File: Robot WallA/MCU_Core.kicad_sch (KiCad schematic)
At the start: 16 parts, among them IC1 STM32F407IGT6, IC2 DS04-254-2-04BK-SMT, J1 Conn_02x05_Female, Y1 Crystal_GND24

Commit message: Correct a lot of error in DRC
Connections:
- net PE2 is gone; now on net LED_Red: IC1.1 (PE2)
- net PE3 is gone; now on net LED_Blue: IC1.2 (PE3)
- net PE4 is gone; now on net LED_Green: IC1.3 (PE4)
- net PE5 is gone; now on net LED_Orange: IC1.4 (PE5)
- net PE6 is gone; now on net LED_Yellow: IC1.5 (PE6)
- no-connect marks 4 -> 8
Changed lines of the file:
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@@
 	)
 	(no_connect
+		(at 68.58 237.49)
+	)
+	(no_connect
 		(at 41.91 116.84)
 	)
@@
 	)
 	(no_connect
+		(at 68.58 234.95)
+	)
+	(no_connect
 		(at 55.88 116.84)
 	)
@@
 		(at 55.88 113.03)
 	)
-	(bus_entry
-		(at 364.49 62.23)
-		(size -2.54 2.54)
-		(stroke
-			(width 0)
-			(type default)
-		)
+	(no_connect
+		(at 68.58 240.03)
+	)
+	(no_connect
+		(at 68.58 242.57)
 	)
 	(bus_entry
@@
 	)
 	(bus_entry
-		(at 364.49 59.69)
-		(size -2.54 2.54)
-		(stroke
-			(width 0)
-			(type default)
-		)
-	)
-	(bus_entry
 		(at 387.35 34.29)
 		(size 2.54 2.54)
@@
 	)
 	(bus_entry
-		(at 364.49 64.77)
-		(size -2.54 2.54)
-		(stroke
-			(width 0)
-			(type default)
-		)
-	)
-	(bus_entry
 		(at 342.9 67.31)
 		(size 2.54 2.54)
@@
 	)
 	(bus_entry
-		(at 364.49 67.31)
-		(size -2.54 2.54)
-		(stroke
-			(width 0)
-			(type default)
-		)
-	)
-	(bus_entry
 		(at 339.09 237.49)
 		(size -2.54 2.54)
@@
 	)
 	(bus_entry
-		(at 364.49 57.15)
-		(size -2.54 2.54)
-		(stroke
-			(width 0)
-			(type default)
-		)
-	)
-	(bus_entry
 		(at 364.49 95.25)
 		(size -2.54 2.54)
@@
 	(wire
 		(pts
-			(xy 360.68 64.77) (xy 361.95 64.77)
-		)
-		(stroke
-			(width 0)
-			(type default)
-		)
-	)
-	(wire
-		(pts
 			(xy 35.56 160.02) (xy 38.1 160.02)
 		)
@@
 	(bus
 		(pts
-			(xy 364.49 64.77) (xy 364.49 67.31)
-		)
-		(stroke
-			(width 0)
-			(type default)
-		)
-	)
-	(bus
-		(pts
 			(xy 365.76 76.2) (xy 364.49 76.2)
 		)
@@
 		)
 	)
-	(wire
-		(pts
-			(xy 360.68 67.31) (xy 361.95 67.31)
-		)
-		(stroke
-			(width 0)
-			(type default)
-		)
-	)
 	(bus
 		(pts
@@
 		)
 	)
-	(bus
-		(pts
-			(xy 364.49 57.15) (xy 364.49 59.69)
-		)
-		(stroke
-			(width 0)
-			(type default)
-		)
-	)
 	(wire
 		(pts
@@
 		)
 	)
-	(bus
-		(pts
-			(xy 364.49 67.31) (xy 364.49 69.85)
-		)
-		(stroke
-			(width 0)
-			(type default)
-		)
-	)
 	(wire
 		(pts
@@
 		)
 	)
-	(wire
-		(pts
-			(xy 360.68 62.23) (xy 361.95 62.23)
-		)
-		(stroke
-			(width 0)
-			(type default)
-		)
-	)
 	(bus
 		(pts
@@
 		)
 	)
-	(bus
-		(pts
-			(xy 364.49 62.23) (xy 364.49 64.77)
-		)
-		(stroke
-			(width 0)
-			(type default)
-		)
-	)
 	(wire
 		(pts
@@
 	(bus
 		(pts
-			(xy 364.49 54.61) (xy 364.49 57.15)
+			(xy 364.49 54.61) (xy 364.49 69.85)
 		)
 		(stroke
@@
 		)
 	)
-	(wire
-		(pts
-			(xy 360.68 69.85) (xy 361.95 69.85)
-		)
-		(stroke
-			(width 0)
-			(type default)
-		)
-	)
 	(bus
 		(pts
@@
 	(bus
 		(pts
-			(xy 364.49 59.69) (xy 364.49 62.23)
-		)
-		(stroke
-			(width 0)
-			(type default)
-		)
-	)
-	(bus
-		(pts
 			(xy 364.49 135.89) (xy 364.49 138.43)
 		)
@@
 	(wire
 		(pts
-			(xy 360.68 59.69) (xy 361.95 59.69)
-		)
-		(stroke
-			(width 0)
-			(type default)
-		)
-	)
-	(wire
-		(pts
 			(xy 354.33 130.81) (xy 361.95 130.81)
 		)
@@
 		)
 	)
-	(label "PE5"
-		(at 360.68 67.31 180)
-		(effects
-			(font
-				(size 1.27 1.27)
-			)
-			(justify right bottom)
-		)
-	)
 	(label "RMII_MDC"
 		(at 227.33 195.58 270)
@@
 	)
 	(label "LED_Blue"
-		(at 52.07 255.27 0)
+		(at 148.59 195.58 270)
 		(effects
 			(font
 				(size 1.27 1.27)
 			)
-			(justify left bottom)
+			(justify right bottom)
 		)
 	)
@@
 	)
 	(label "LED_Orange"
-		(at 52.07 260.35 0)
+		(at 153.67 195.58 270)
 		(effects
 			(font
 				(size 1.27 1.27)
 			)
-			(justify left bottom)
+			(justify right bottom)
 		)
 	)
@@
 		)
 	)
-	(label "PE6"
-		(at 156.21 195.58 270)
-		(effects
-			(font
-				(size 1.27 1.27)
-			)
-			(justify right bottom)
-		)
-	)
 	(label "PH8"
 		(at 278.13 86.36 0)
@@
 		)
 	)
-	(label "PE3"
-		(at 360.68 62.23 180)
-		(effects
-			(font
-				(size 1.27 1.27)
-			)
-			(justify right bottom)
-		)
-	)
 	(label "VDD"
 		(at 234.95 195.58 270)
@@
 		)
 	)
-	(label "PE4"
-		(at 360.68 64.77 180)
-		(effects
-			(font
-				(size 1.27 1.27)
-			)
-			(justify right bottom)
-		)
-	)
 	(label "PHY_CLK_25MHZ"
 		(at 179.07 71.12 90)
@@
 		)
 	)
-	(label "PE2"
-		(at 360.68 59.69 180)
-		(effects
-			(font
-				(size 1.27 1.27)
-			)
-			(justify right bottom)
-		)
-	)
 	(label "ETH1"
 		(at 360.68 123.19 180)
@@
 	)
 	(label "LED_Green"
-		(at 52.07 250.19 0)
+		(at 151.13 195.58 270)
 		(effects
 			(font
 				(size 1.27 1.27)
 			)
-			(justify left bottom)
+			(justify right bottom)
 		)
 	)
@@
 	)
 	(label "LED_Yellow"
-		(at 52.07 257.81 0)
+		(at 156.21 195.58 270)
 		(effects
 			(font
 				(size 1.27 1.27)
 			)
-			(justify left bottom)
+			(justify right bottom)
 		)
 	)
@@
 		)
 	)
-	(label "PE6"
-		(at 360.68 69.85 180)
-		(effects
-			(font
-				(size 1.27 1.27)
-			)
-			(justify right bottom)
-		)
-	)
 	(label "PF3"
 		(at 191.77 195.58 270)
@@
 		)
 	)
-	(label "PE3"
-		(at 148.59 195.58 270)
-		(effects
-			(font
-				(size 1.27 1.27)
-			)
-			(justify right bottom)
-		)
-	)
 	(label "Sensor_InputCapture4"
 		(at 181.61 71.12 90)
@@
 		)
 	)
-	(label "PE2"
-		(at 146.05 195.58 270)
-		(effects
-			(font
-				(size 1.27 1.27)
-			)
-			(justify right bottom)
-		)
-	)
 	(label "SWCLK"
 		(at 128.27 88.9 180)
@@
 		)
 	)
-	(label "PE5"
-		(at 153.67 195.58 270)
-		(effects
-			(font
-				(size 1.27 1.27)
-			)
-			(justify right bottom)
-		)
-	)
 	(label "PD14"
 		(at 346.71 69.85 0)
@@
 	)
 	(label "LED_Red"
-		(at 52.07 252.73 0)
+		(at 146.05 195.58 270)
 		(effects
 			(font
 				(size 1.27 1.27)
 			)
-			(justify left bottom)
+			(justify right bottom)
 		)
 	)
@@
 		(effects
 			(font
-				(size 1.27 1.27)
-			)
-			(justify right bottom)
-		)
-	)
-	(label "PE4"
-		(at 151.13 195.58 270)
-		(effects
-			(font

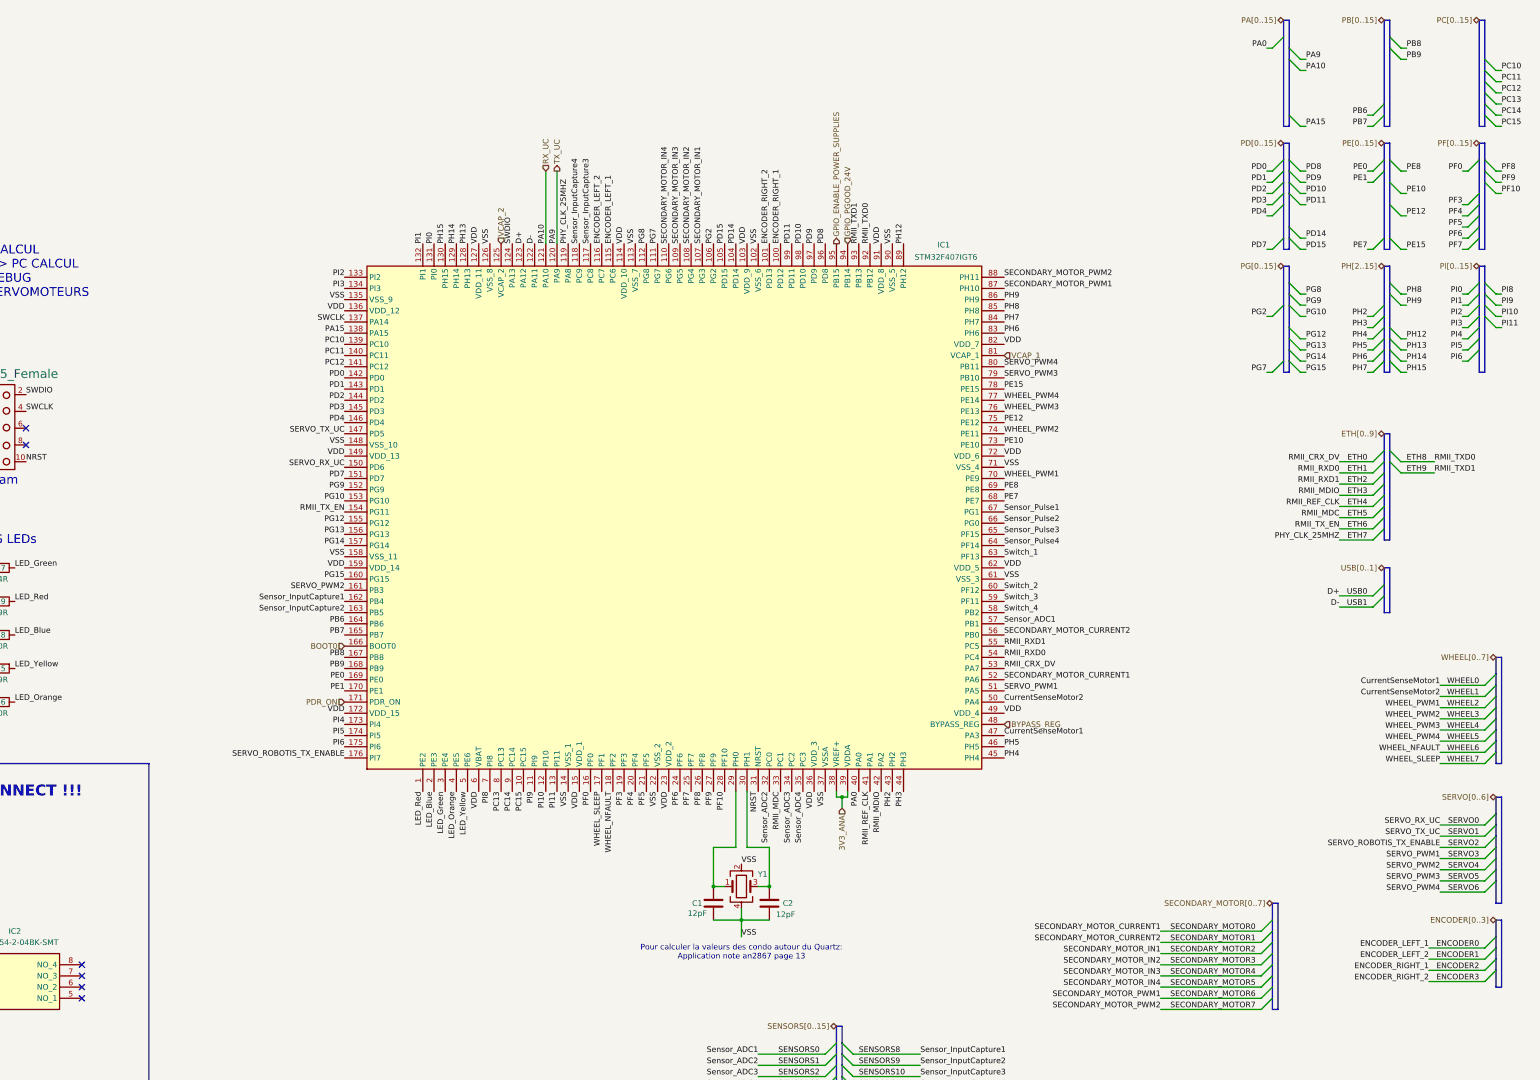
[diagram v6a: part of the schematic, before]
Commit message: Corrected all DRC erros, added info on PCB
modified distance meter connectors to be horizontal
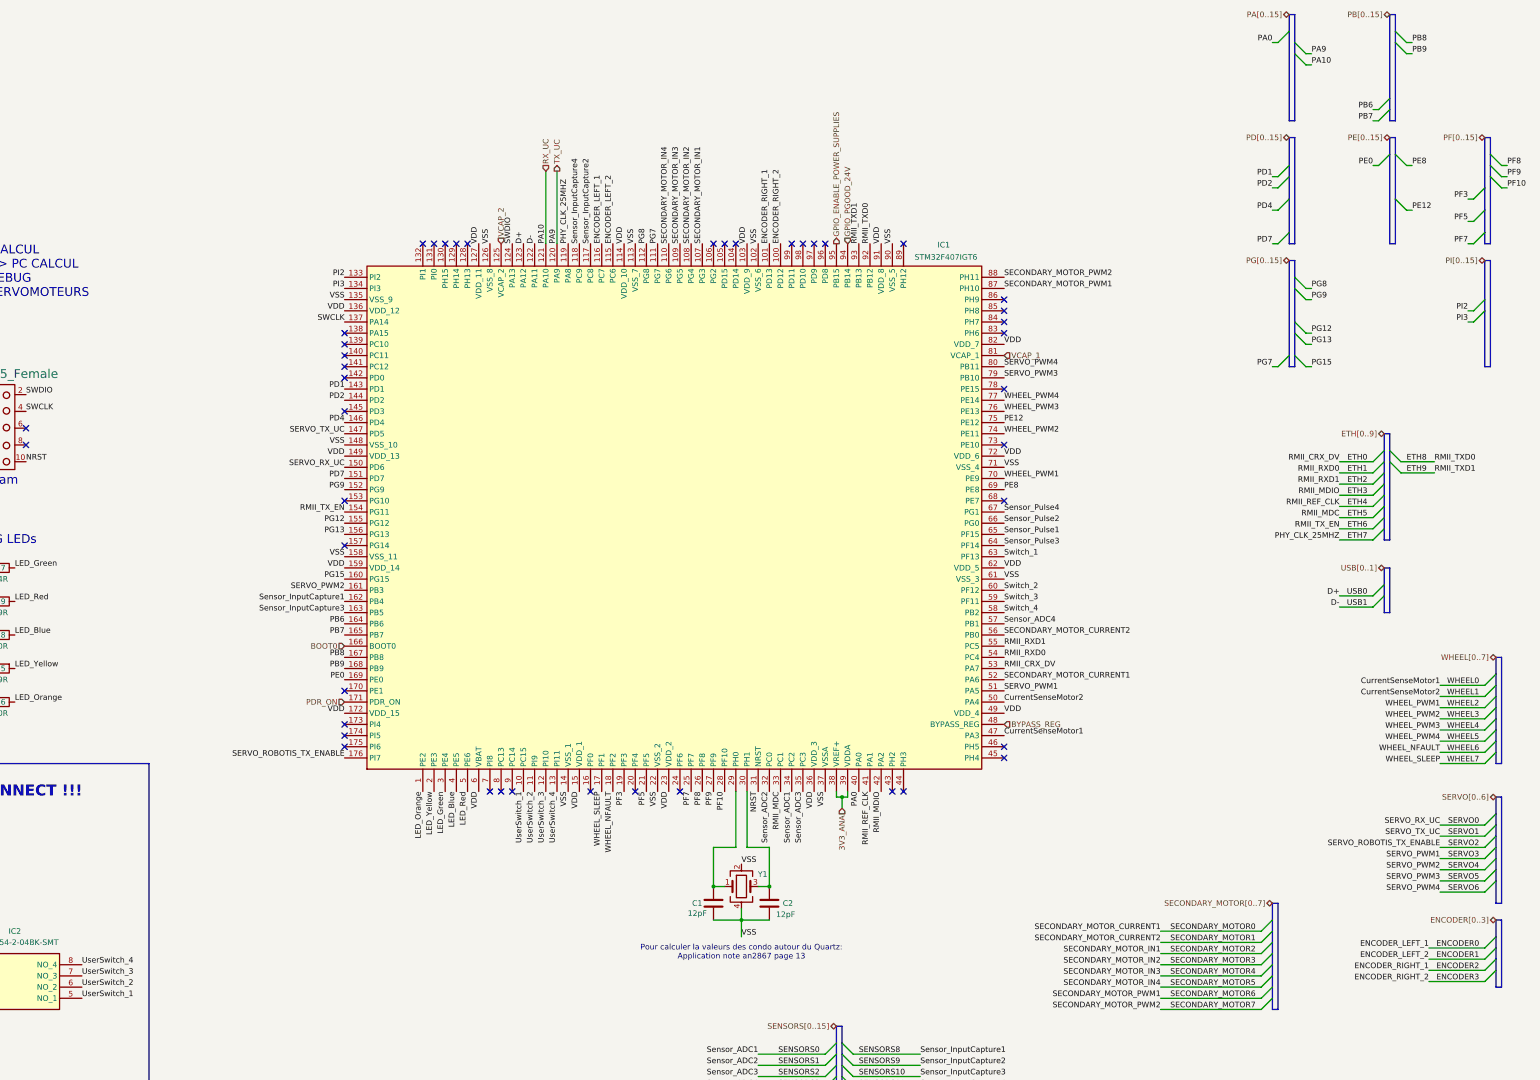
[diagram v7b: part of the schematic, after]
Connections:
- net PC15 is gone; now on net UserSwitch_1: IC1.10 (PC15)
- net PI10 is gone; now on net UserSwitch_3: IC1.12 (PI10)
- net PI11 is gone; now on net UserSwitch_4: IC1.13 (PI11)
- net PI9 is gone; now on net UserSwitch_2: IC1.11 (PI9)
- net ENCODER0: now also IC1.116 (PC7); no longer IC1.115 (PC6)
- net ENCODER1: now also IC1.115 (PC6); no longer IC1.116 (PC7)
- net ENCODER2: now also IC1.101 (PD13); no longer IC1.100 (PD12)
- net ENCODER3: now also IC1.100 (PD12); no longer IC1.101 (PD13)
- net LED_Blue: now also IC1.4 (PE5); no longer IC1.2 (PE3)
- net LED_Orange: now also IC1.1 (PE2); no longer IC1.4 (PE5)
- net LED_Red: now also IC1.5 (PE6); no longer IC1.1 (PE2)
- net LED_Yellow: now also IC1.2 (PE3); no longer IC1.5 (PE6)
- net SENSORS0: now also IC1.34 (PC2); no longer IC1.57 (PB1)
- net SENSORS10: now also IC1.163 (PB5); no longer IC1.117 (PC8)
- net SENSORS2: now also IC1.35 (PC3); no longer IC1.34 (PC2)
- net SENSORS3: now also IC1.57 (PB1); no longer IC1.35 (PC3)
- net SENSORS4: now also IC1.65 (PF15); no longer IC1.67 (PG1)
- net SENSORS6: now also IC1.64 (PF14); no longer IC1.65 (PF15)
- net SENSORS7: now also IC1.67 (PG1); no longer IC1.64 (PF14)
- net SENSORS9: now also IC1.117 (PC8); no longer IC1.163 (PB5)
- net UserSwitch_1: now reaches IC2.5 (NO_1)
- net UserSwitch_2: now reaches IC2.6 (NO_2)
- net UserSwitch_3: now reaches IC2.7 (NO_3)
- net UserSwitch_4: now reaches IC2.8 (NO_4)
- net PA15: no longer names the net of IC1.138 (PA15)
- net PC10: no longer names the net of IC1.139 (PC10)
- net PC11: no longer names the net of IC1.140 (PC11)
- net PC12: no longer names the net of IC1.141 (PC12)
- net PC13: no longer names the net of IC1.8 (PC13)
- net PC14: no longer names the net of IC1.9 (PC14)
- net PD0: no longer names the net of IC1.142 (PD0)
- net PD10: no longer names the net of IC1.98 (PD10)
- net PD11: no longer names the net of IC1.99 (PD11)
- net PD14: no longer names the net of IC1.104 (PD14)
- net PD15: no longer names the net of IC1.105 (PD15)
- net PD3: no longer names the net of IC1.145 (PD3)
- net PD8: no longer names the net of IC1.96 (PD8)
- net PD9: no longer names the net of IC1.97 (PD9)
- net PE1: no longer names the net of IC1.170 (PE1)
- net PE10: no longer names the net of IC1.73 (PE10)
- net PE15: no longer names the net of IC1.78 (PE15)
- net PE7: no longer names the net of IC1.68 (PE7)
- net PF0: no longer names the net of IC1.16 (PF0)
- net PF4: no longer names the net of IC1.20 (PF4)
- net PF6: no longer names the net of IC1.24 (PF6)
- net PG10: no longer names the net of IC1.153 (PG10)
- net PG14: no longer names the net of IC1.157 (PG14)
- net PG2: no longer names the net of IC1.106 (PG2)
- net PH12: no longer names the net of IC1.89 (PH12)
- net PH13: no longer names the net of IC1.128 (PH13)
- net PH14: no longer names the net of IC1.129 (PH14)
- net PH15: no longer names the net of IC1.130 (PH15)
- net PH2: no longer names the net of IC1.43 (PH2)
- net PH3: no longer names the net of IC1.44 (PH3)
- net PH4: no longer names the net of IC1.45 (PH4)
- net PH5: no longer names the net of IC1.46 (PH5)
- net PH6: no longer names the net of IC1.83 (PH6)
- net PH7: no longer names the net of IC1.84 (PH7)
- net PH8: no longer names the net of IC1.85 (PH8)
- net PH9: no longer names the net of IC1.86 (PH9)
- net PI0: no longer names the net of IC1.131 (PI0)
- net PI1: no longer names the net of IC1.132 (PI1)
- net PI4: no longer names the net of IC1.173 (PI4)
- net PI5: no longer names the net of IC1.174 (PI5)
- net PI6: no longer names the net of IC1.175 (PI6)
- net PI8: no longer names the net of IC1.7 (PI8)
- no-connect marks 8 -> 46

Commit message: Updated fab files.
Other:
- company: (none) -> Socotec Monitoring
- title: (none) -> Robot Wall-A
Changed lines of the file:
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@@
 	(generator_version "9.0")
 	(paper "A3")
+	(title_block
+		(title "Robot Wall-A")
+		(date "2025-09-20")
+		(rev "v1.0")
+		(company "Socotec Monitoring")
+		(comment 1 "GDU")
+		(comment 2 "THO")
+	)
 	(rectangle
 		(start 16.51 189.23)
@@
 			)
 		)
+		(property "MPN" ""
+			(at 212.09 220.98 0)
+			(effects
+				(font
+					(size 1.27 1.27)
+				)
+				(hide yes)
+			)
+		)
 		(pin "1"
 		)
@@
 			)
 		)
+		(property "MPN" ""
+			(at 41.91 167.64 0)
+			(effects
+				(font
+					(size 1.27 1.27)
+				)
+				(hide yes)
+			)
+		)
 		(pin "2"
 		)
@@
 			)
 		)
+		(property "MPN" ""
+			(at 49.53 160.02 90)
+			(effects
+				(font
+					(size 1.27 1.27)
+				)
+				(hide yes)
+			)
+		)
 		(pin "1"
 		)
@@
 			)
 		)
+		(property "MPN" ""
+			(at 41.91 175.26 0)
+			(effects
+				(font
+					(size 1.27 1.27)
+				)
+				(hide yes)
+			)
+		)
 		(pin "2"
 		)
@@
 			)
 		)
+		(property "MPN" ""
+			(at 38.1 234.95 0)
+			(effects
+				(font
+					(size 1.27 1.27)
+				)
+				(hide yes)
+			)
+		)
 		(pin "1"
 		)
@@
 			)
 		)
+		(property "MPN" ""
+			(at 41.91 152.4 0)
+			(effects
+				(font
+					(size 1.27 1.27)
+				)
+				(hide yes)
+			)
+		)
 		(pin "2"
 		)
@@
 			)
 		)
+		(property "MPN" ""
+			(at 224.79 220.98 0)
+			(effects
+				(font
+					(size 1.27 1.27)
+				)
+				(hide yes)
+			)
+		)
 		(pin "1"
 		)
@@
 			)
 		)
+		(property "MPN" ""
+			(at 49.53 175.26 90)
+			(effects
+				(font
+					(size 1.27 1.27)
+				)
+				(hide yes)
+			)
+		)
 		(pin "2"
 		)
@@
 			)
 		)
+		(property "MPN" ""
+			(at 49.53 167.64 90)
+			(effects
+				(font
+					(size 1.27 1.27)
+				)
+				(hide yes)
+			)
+		)
 		(pin "2"
 		)
@@
 			)
 		)
+		(property "MPN" ""
+			(at 41.91 144.78 0)
+			(effects
+				(font
+					(size 1.27 1.27)
+				)
+				(hide yes)
+			)
+		)
 		(pin "2"
 		)
@@
 			)
 		)
+		(property "MPN" ""
+			(at 49.53 96.52 0)
+			(effects
+				(font
+					(size 1.27 1.27)
+				)
+				(hide yes)
+			)
+		)
 		(pin "1"
 		)
@@
 			)
 		)
+		(property "MPN" ""
+			(at 49.53 144.78 90)
+			(effects
+				(font
+					(size 1.27 1.27)
+				)
+				(hide yes)
+			)
+		)
 		(pin "1"
 		)
@@
 			)
 		)
+		(property "MPN" ""
+			(at 218.44 217.17 0)
+			(effects
+				(font
+					(size 1.27 1.27)
+				)
+				(hide yes)
+			)
+		)
 		(pin "1"
 		)
@@
 			)
 		)
+		(property "MPN" ""
+			(at 49.53 152.4 90)
+			(effects
+				(font
+					(size 1.27 1.27)
+				)
+				(hide yes)
+			)
+		)
 		(pin "1"
 		)
@@
 			)
 		)
+		(property "MPN" ""
+			(at 41.91 160.02 0)
+			(effects
+				(font
+					(size 1.27 1.27)
+				)
+				(hide yes)
+			)
+		)
 		(pin "2"
 		)
@@
 				(hide yes)
 			)
+		)
+		(property "MPN" ""
+			(at 146.05 195.58 90)
+			(effects
+				(font
+					(size 1.27 1.27)
+				)
+				(hide yes)
+			)
